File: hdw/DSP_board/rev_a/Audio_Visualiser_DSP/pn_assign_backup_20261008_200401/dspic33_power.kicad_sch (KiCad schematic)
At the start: 30 parts, among them J1401 Left, J1402 Right, J1403 Speaker Left TP, J1404 Speaker Right TP, U1401 MCP6N11-001, U1402 MCP6N11-001

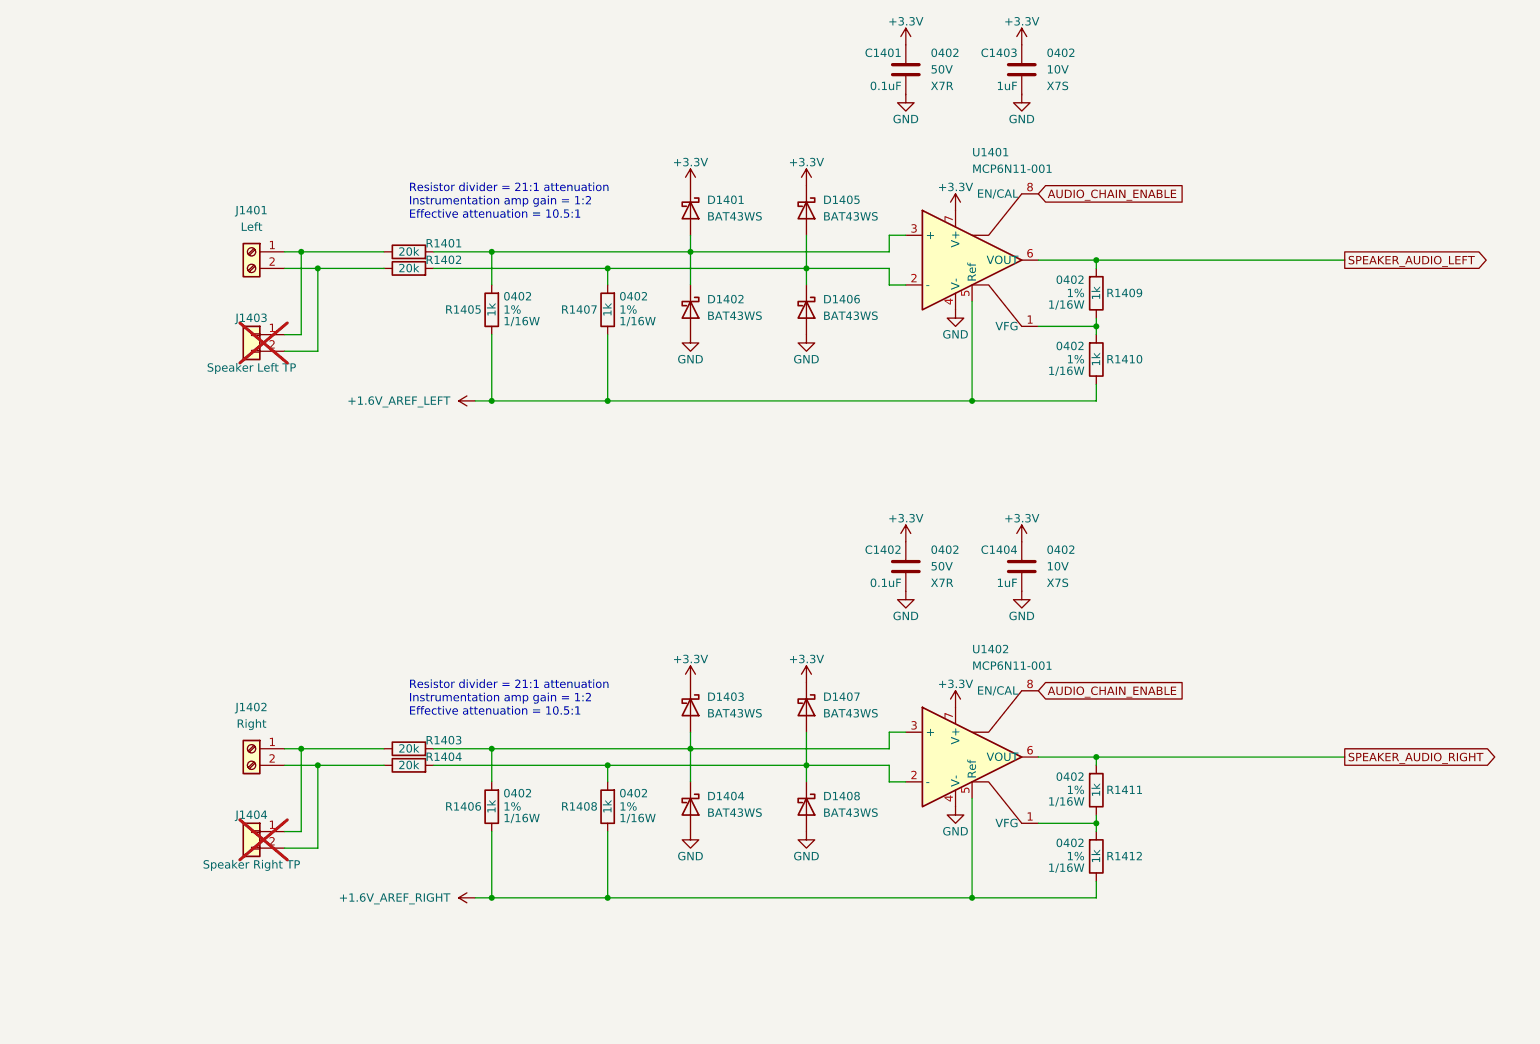
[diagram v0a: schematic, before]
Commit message: fix a lot of digikey pns which are out of stock, find alternate inductors, change I2C buffers
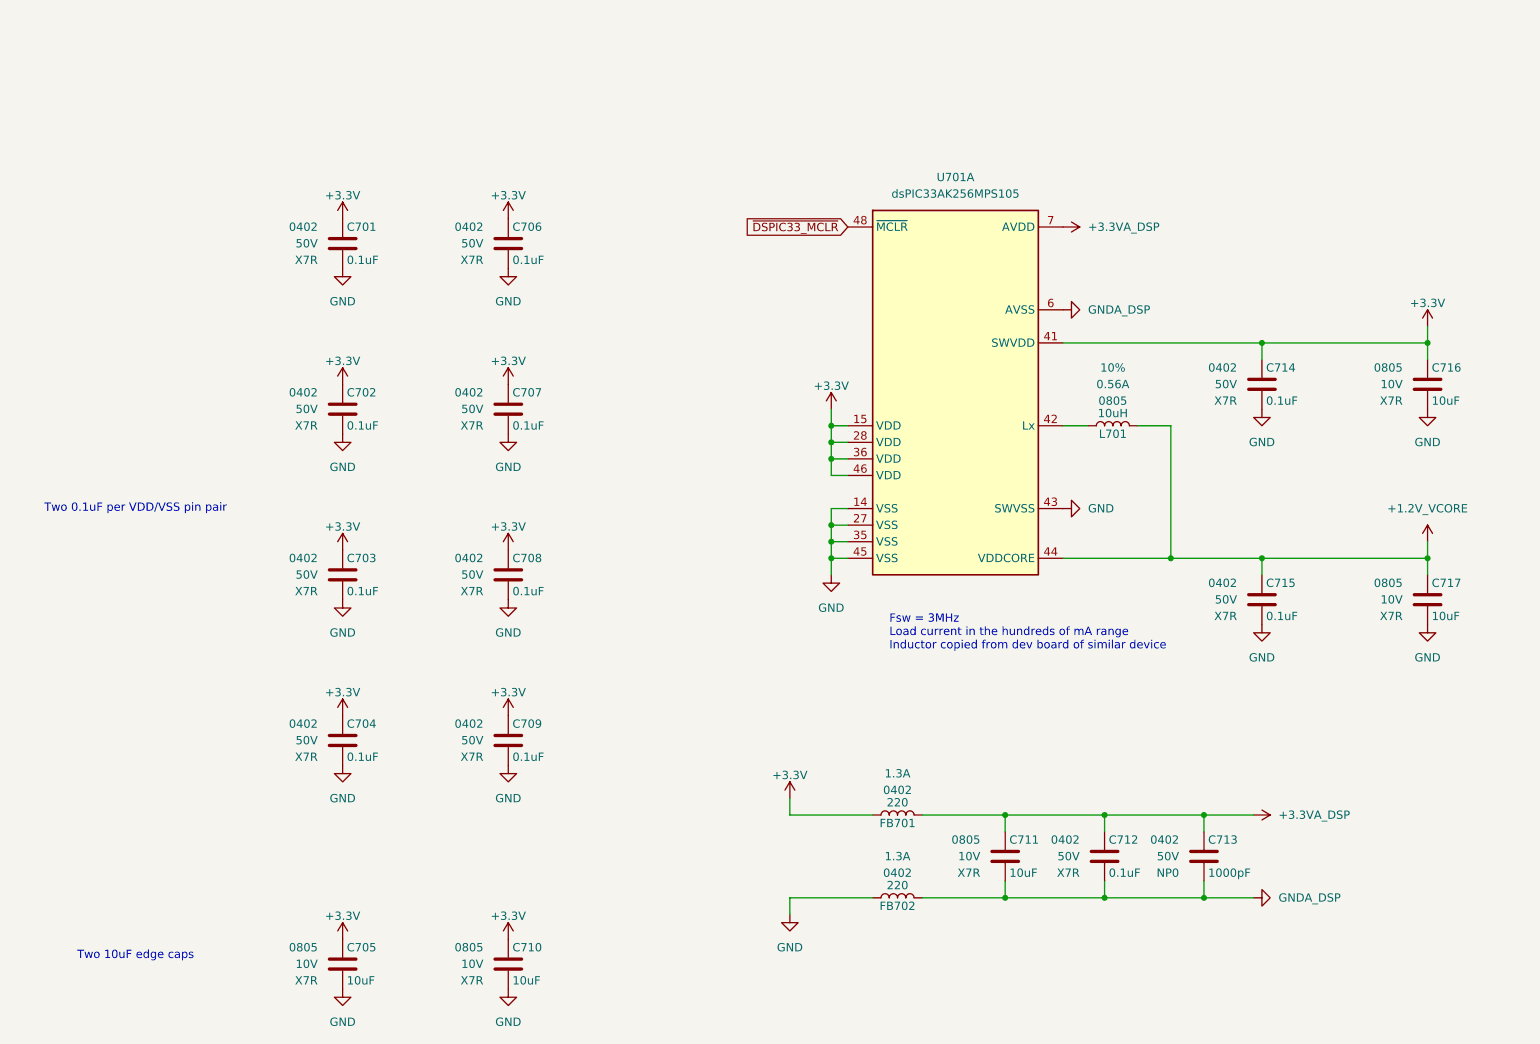
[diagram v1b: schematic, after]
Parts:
- removed C1401, C1402: 0.1uF, Capacitors_SMD:C_0402, symbol Custom_Library:C_Custom
- removed C1403, C1404: 1uF, Capacitors_SMD:C_0402, symbol Custom_Library:C_Custom
- removed D1401, D1402, D1403, D1404, D1405, D1406, D1407, D1408: BAT43WS, Diode_SMD:D_SOD-323F, symbol Diode:BAT54J
- removed J1401: Left, TerminalBlock_Phoenix:TerminalBlock_Phoenix_MKDS-1,5-2-5.08_1x02_P5.08mm_Horizontal, symbol Connector:Screw_Terminal_01x02
- removed J1402: Right, TerminalBlock_Phoenix:TerminalBlock_Phoenix_MKDS-1,5-2-5.08_1x02_P5.08mm_Horizontal, symbol Connector:Screw_Terminal_01x02
- removed J1403: Speaker Left TP, Connector_PinSocket_2.54mm:PinSocket_1x02_P2.54mm_Vertical, symbol Connector_Generic:Conn_01x02
- removed J1404: Speaker Right TP, Connector_PinSocket_2.54mm:PinSocket_1x02_P2.54mm_Vertical, symbol Connector_Generic:Conn_01x02
- removed R1401, R1402, R1403, R1404: 20k, Resistors_SMD:R_0402, symbol Custom Library:R_Custom
- removed R1405, R1406, R1407, R1408, R1409, R1410, R1411, R1412: 1k, Resistors_SMD:R_0402, symbol Custom_Library:R_Custom
- removed U1401, U1402: MCP6N11-001, Package_DFN_QFN:DFN-8-1EP_3x2mm_P0.5mm_EP1.36x1.46mm, symbol MCP6N11:MCP6N11-001
- added C701, C702, C703, C704, C706, C707, C708, C709, C712, C714, C715: 0.1uF, Capacitors_SMD:C_0402, symbol Custom Library:C_Custom
- added C705, C710, C711, C716, C717: 10uF, Capacitors_SMD:C_0805, symbol Custom Library:C_Custom
- added C713: 1000pF, Capacitors_SMD:C_0402, symbol Custom Library:C_Custom
- added FB701, FB702: 220, Inductors_SMD:L_0402, symbol Custom Library:FB_Custom
- added L701: 10uH, Inductors_SMD:L_0805, symbol Custom Library:L_Custom
- added U701: dsPIC33AK256MPS105, Package_DFN_QFN:VQFN-48-1EP_6x6mm_P0.4mm_EP4.1x4.1mm, symbol dsPIC33AK256MPS105:dsPIC33AK256MPS105
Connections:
- net +3.3V: now also C701.1, C702.1, C703.1, C704.1, C705.1, C706.1, C707.1, C708.1, C709.1, C710.1, C714.1, C716.1, FB701.1, U701.15 (VDD), U701.28 (VDD), U701.36 (VDD), U701.41 (SWVDD), U701.46 (VDD)
- net GND: now also C701.2, C702.2, C703.2, C704.2, C705.2, C706.2, C707.2, C708.2, C709.2, C710.2, C714.2, C715.2, C716.2, C717.2, FB702.1, U701.14 (VSS), U701.27 (VSS), U701.35 (VSS), U701.43 (SWVSS), U701.45 (VSS), U701.49 (VSS)
- new net: L701.1, U701.42 (Lx)
- new net +1.2V_VCORE: C715.1, C717.1, L701.2, U701.44 (VDDCORE)
- new net +3.3VA_DSP: C711.1, C712.1, C713.1, FB701.2, U701.7 (AVDD)
- new net GNDA_DSP: C711.2, C712.2, C713.2, FB702.2, U701.6 (AVSS)
- new net ~{DSPIC33_MCLR}: U701.48 (~{MCLR})
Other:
- note added: "Fsw = 3MHz Load current in the hundreds of mA range Inductor copied from dev board of similar device"
- note added: "Two 0.1uF per VDD/VSS pin pair"
- note added: "Two 10uF edge caps"
- note removed: "Resistor divider = 21:1 attenuation Instrumentation amp gain = 1:2 Effective attenuation = 10.5:1"
